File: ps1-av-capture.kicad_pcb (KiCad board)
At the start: 4 copper layers, 100 x 80 mm, 237 parts, among them J1 AV_PIGTAIL, J2 USB3_B, J3 USB_C_AUDIO, J4 JTAG, J5 UART, SW1 RESET, U1 TVP7002PZP, U10 TLV75733PDBVR, U11 TLV75533PDBVR, U12 PCM2903CDBR, U2 CYUSB3014-BZXI, U3 24LC1025-I/SN, U4 24LC1025-I/SN, U5 TPS563201DDCR, U6 TPS563201DDCR, U7 TPS563201DDCR, U8 TLV75519PDBVR, U9 TLV75519PDBVR, X1 27MHz, Y1 19.2MHz, Y2 12MHz

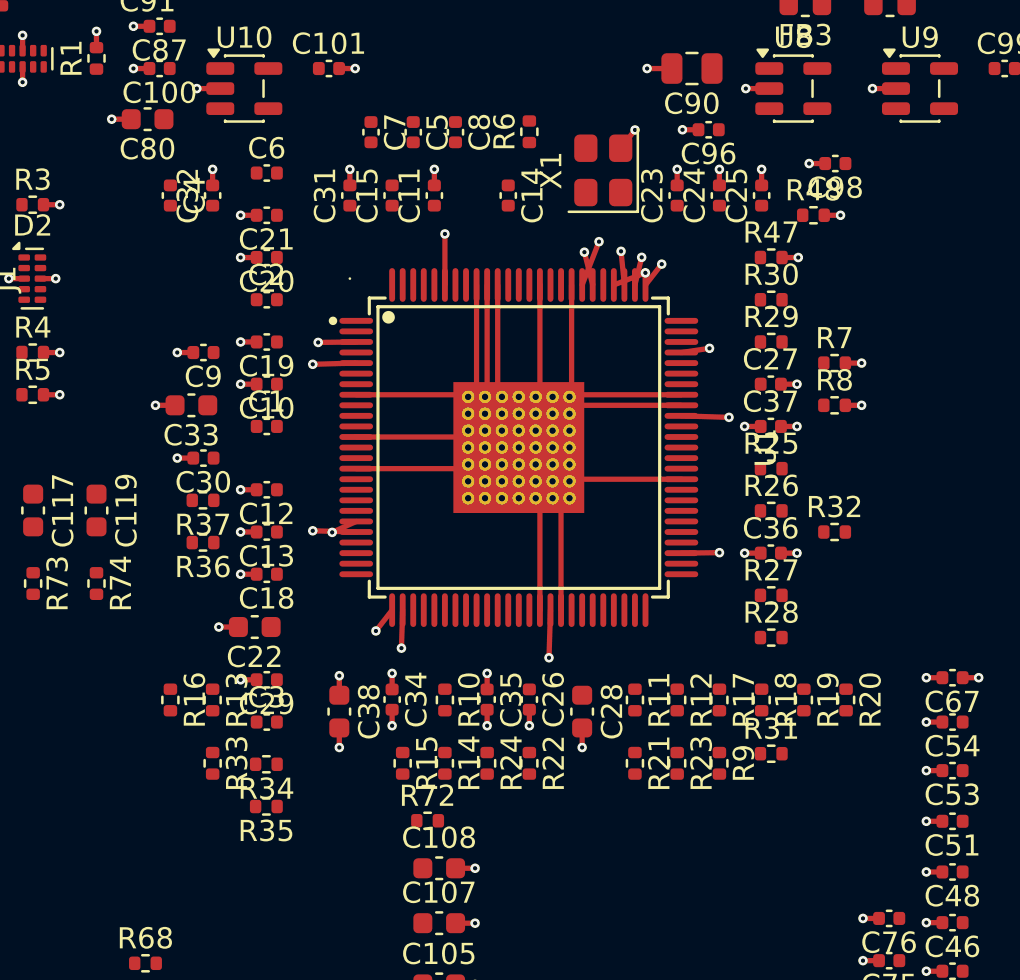
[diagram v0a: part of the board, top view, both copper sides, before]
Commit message: Layout: 22R series terminations hand-placed in pin order
The autoplacer scattered the 34 data/sync terminations around U1, some on the
far side from U2. They now sit just outside U1's escape ring in pin order (B/G
and DATACLK in a row under the south pins, R in a column east, syncs west), so
each bus fans out on L1 with no crossings before the scripted GPIF run.
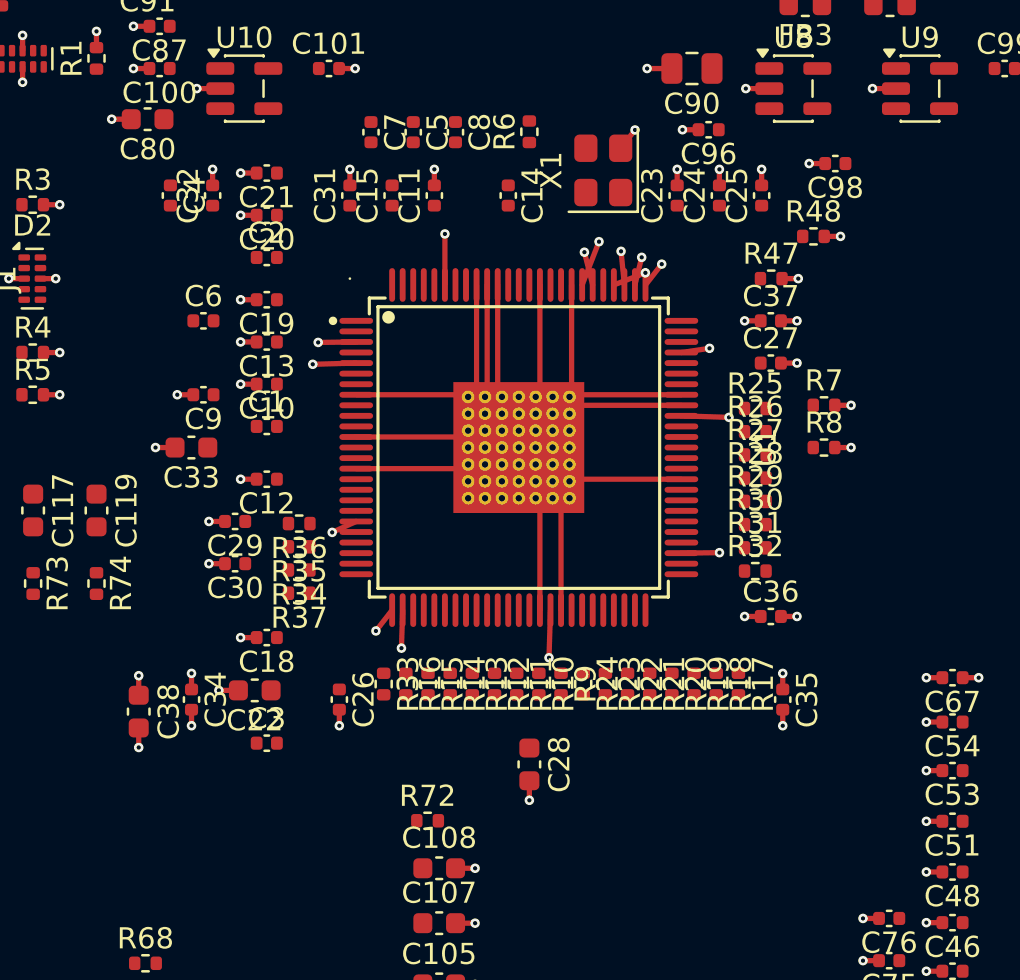
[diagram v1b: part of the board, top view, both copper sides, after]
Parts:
- moved C35 14.0 mm to (145.5, 137.9)
- moved R35 12.4 mm to (122.6, 130.7)
- moved R13 12.3 mm to (130.8, 137.2)
- moved R16 11.2 mm to (127.7, 137.2)
- moved R30 10.7 mm to (144.2, 129.7)
- moved R31 9.78 mm to (144.2, 130.8)
- moved C34 9.50 mm to (117.5, 137.9)
- moved C38 9.50 mm to (115.0, 138.5)
- moved R34 9.33 mm to (122.6, 131.8)
- moved C13 9.00 mm to (121.1, 121.0)
- moved C26 9.00 mm to (124.5, 137.9)
- moved R33 8.93 mm to (126.6, 137.2)
- moved R12 8.68 mm to (131.8, 137.2)
- moved R9 8.39 mm to (135.0, 137.2)
- moved R20 8.28 mm to (140.2, 137.2)
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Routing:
- net GND: track 235.9 -> 233.9 mm, vias 178 -> 177

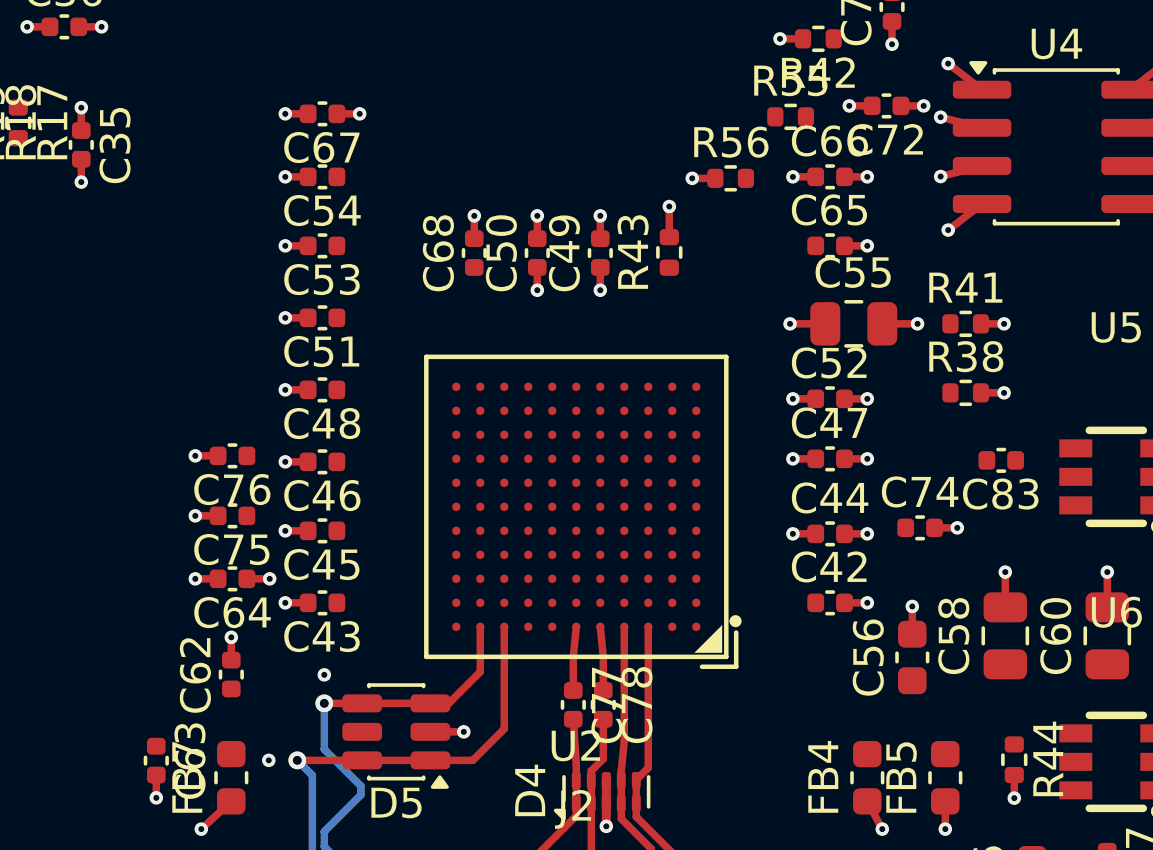
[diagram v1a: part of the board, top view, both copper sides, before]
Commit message: Layout: U2 plane decoupling on B.Cu
The 16 plane-only 0402 caps around the FX3 move to the back at the same spot,
so the F.Cu ring around U2 is free for the BGA escape and the GPIF bundle.
fanout.py stubs a back-side pad on B.Cu.
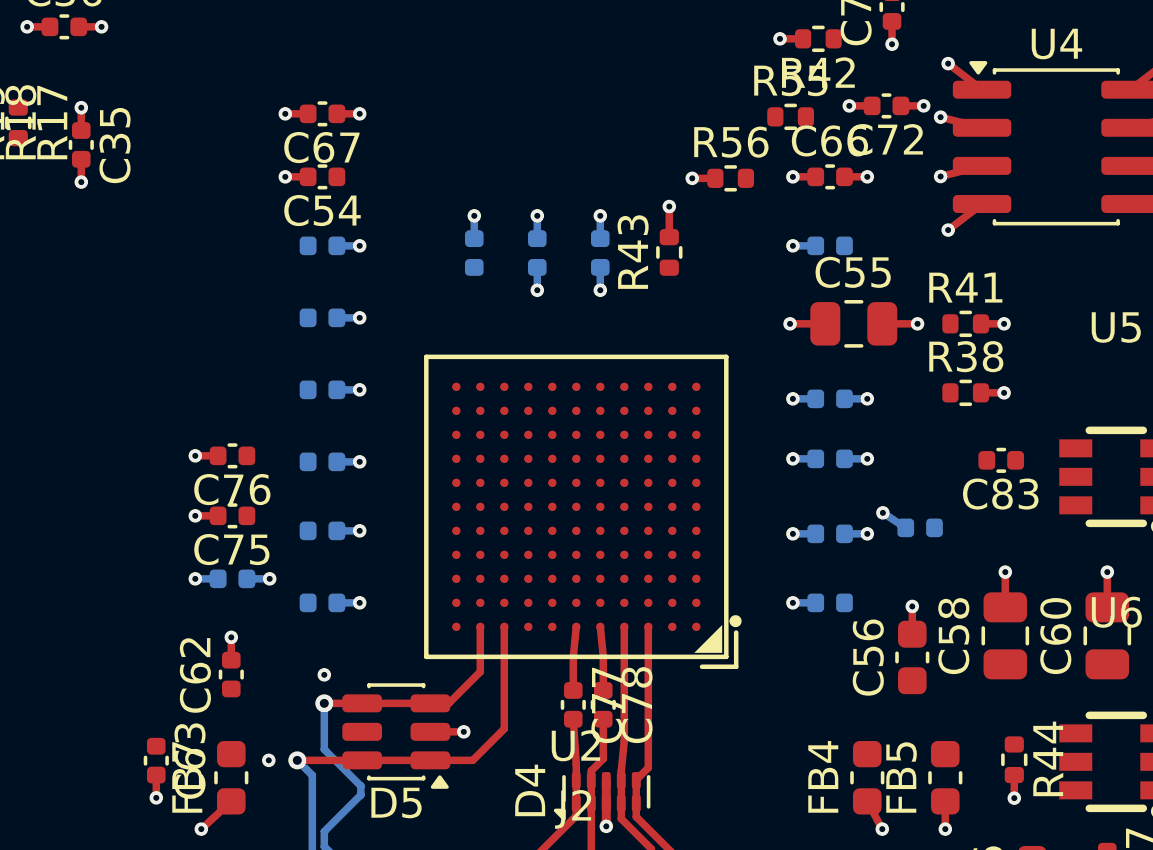
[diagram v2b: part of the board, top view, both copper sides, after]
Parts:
- C42, C43, C44, C45, C46, C47, C48, C49, C50, C51, C52, C53, C64, C65, C68, C74: moved to B.Cu
- turned C42 to 180 degrees
- turned C43 to 0 degrees
- turned C44 to 180 degrees
- turned C45 to 0 degrees
- turned C46 to 0 degrees
- turned C47 to 180 degrees
- turned C48 to 0 degrees
- turned C51 to 0 degrees
- turned C52 to 180 degrees
- turned C53 to 0 degrees
- turned C64 to 0 degrees
- turned C65 to 180 degrees
- turned C74 to 180 degrees

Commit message: Layout: +1V2 island reaches the west decaps
The +1V2 L3 region now starts at x=51 so the back-side +1V2 caps west of U2
can drop their vias onto it. Fanout leaves 41 pads for the router (was 47).
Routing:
- net +1V2: track 12.5 -> 18.5 mm, vias 12 -> 19

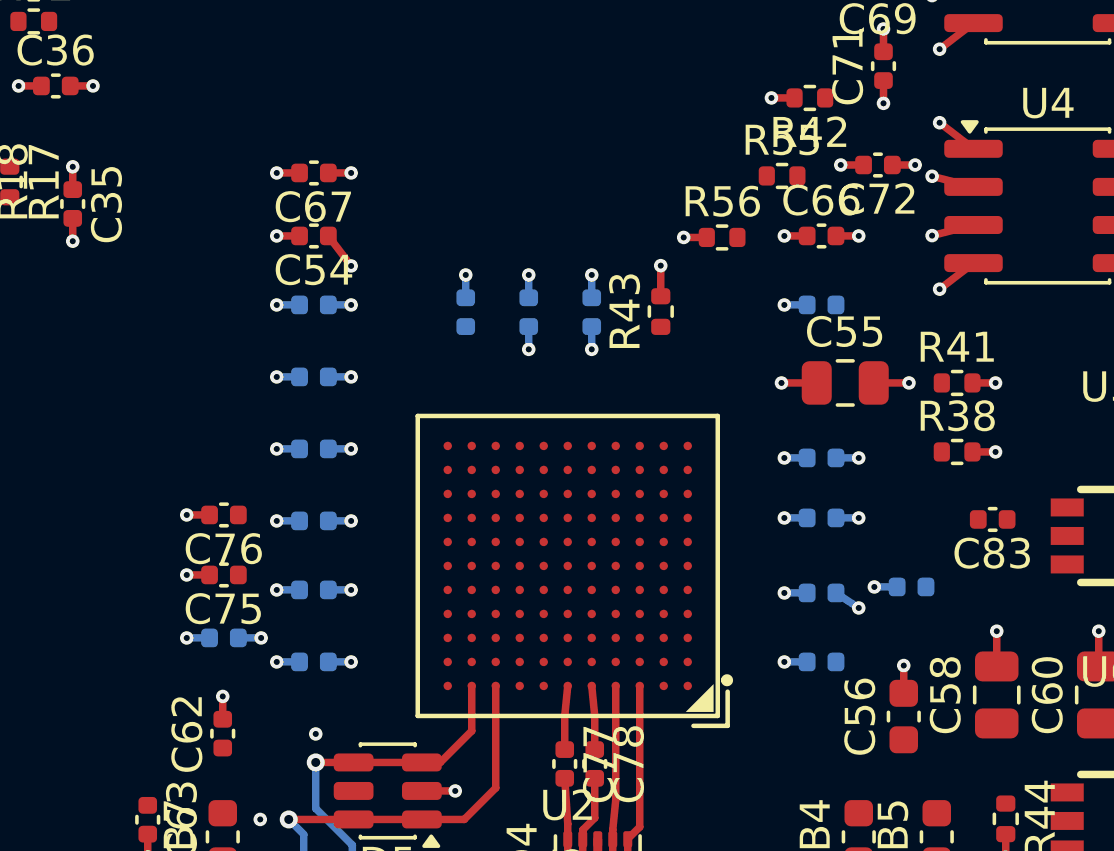
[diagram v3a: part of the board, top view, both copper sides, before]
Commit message: Layout: U2's +3V3 decaps out of the +1V2 island
Five back-side +3V3 caps sat where L3 is +1V2, so their vias had nothing to
land on. They now sit in a row just north of the island, +3V3 pad up. Every
decap around U2 reaches its planes; fanout leaves 37 pads for the router.
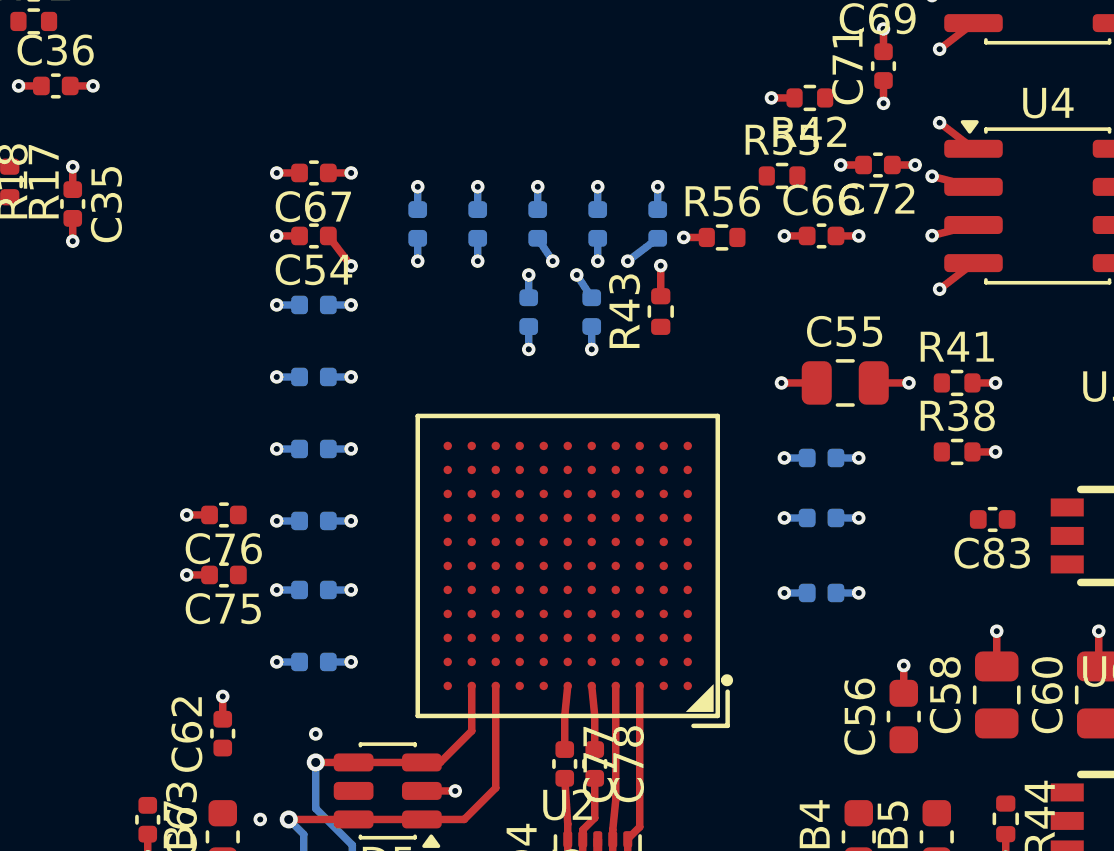
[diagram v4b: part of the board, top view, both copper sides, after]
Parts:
- moved C74 20.4 mm to (157.0, 138.6), turned to -90 degrees
- moved C64 18.6 mm to (163.0, 138.6), turned to -90 degrees
- moved C42 15.6 mm to (165.0, 138.6), turned to -90 degrees
- moved C65 9.84 mm to (161.0, 138.6), turned to -90 degrees
- moved C68 2.97 mm to (159.0, 138.6), turned to -90 degrees
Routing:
- net +3V3: track 40.8 -> 43.9 mm, vias 37 -> 41
- net GND: track 233.9 -> 234.7 mm

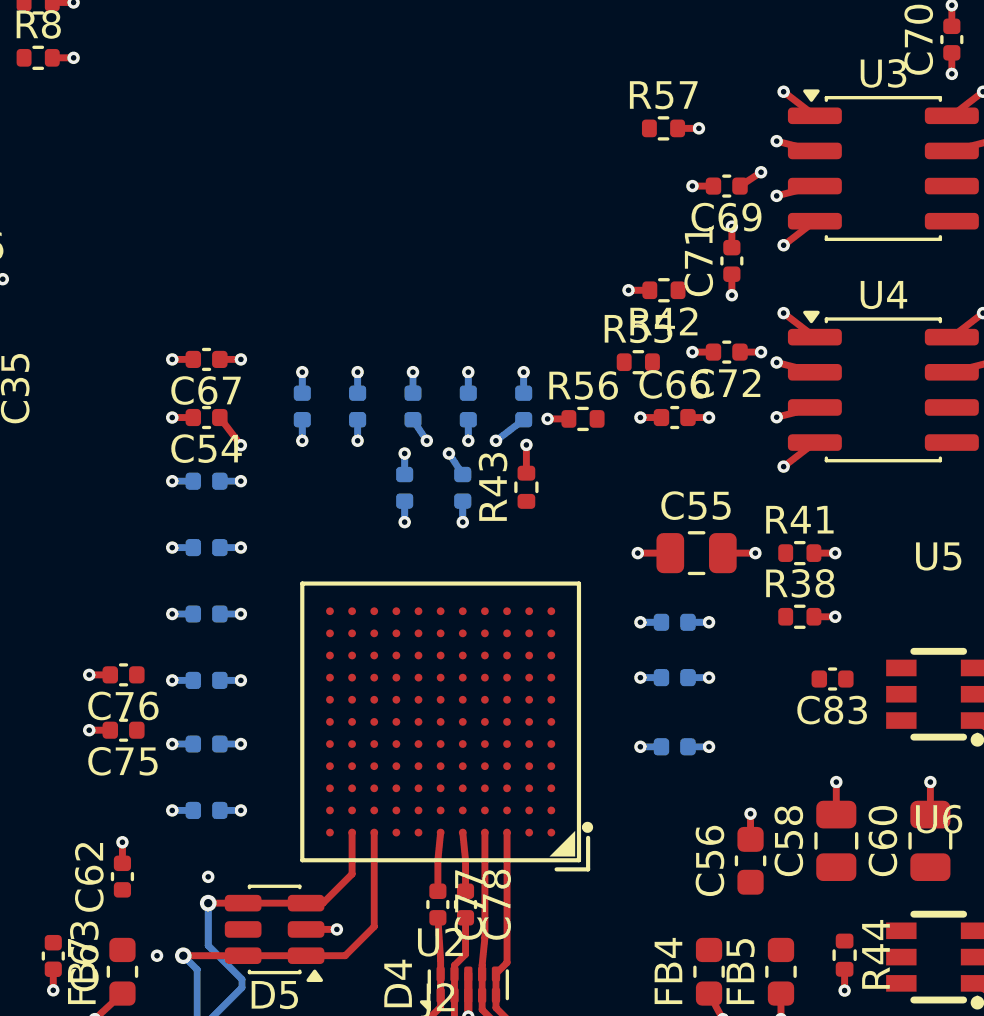
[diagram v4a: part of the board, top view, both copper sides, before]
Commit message: Layout: FX3 plane balls fanned out, +3V3 channels through the +1V2 island
fanout.py counted BGA balls as vias in its same-net hole-to-hole check, so
every dogbone was rejected by its own ball (0.57 mm < 0.7 mm) and no U2 plane
ball was ever fanned. The spacing check now covers vias only: fanout leaves 7
pads for the router (was 37).

U2's six +3V3 balls sit over the L3 +1V2 island; each one's dogbone via now
lands in a +3V3 channel running out past the island edge to the main pour.
DRC lists no unconnected +3V3 or U2 plane pad.
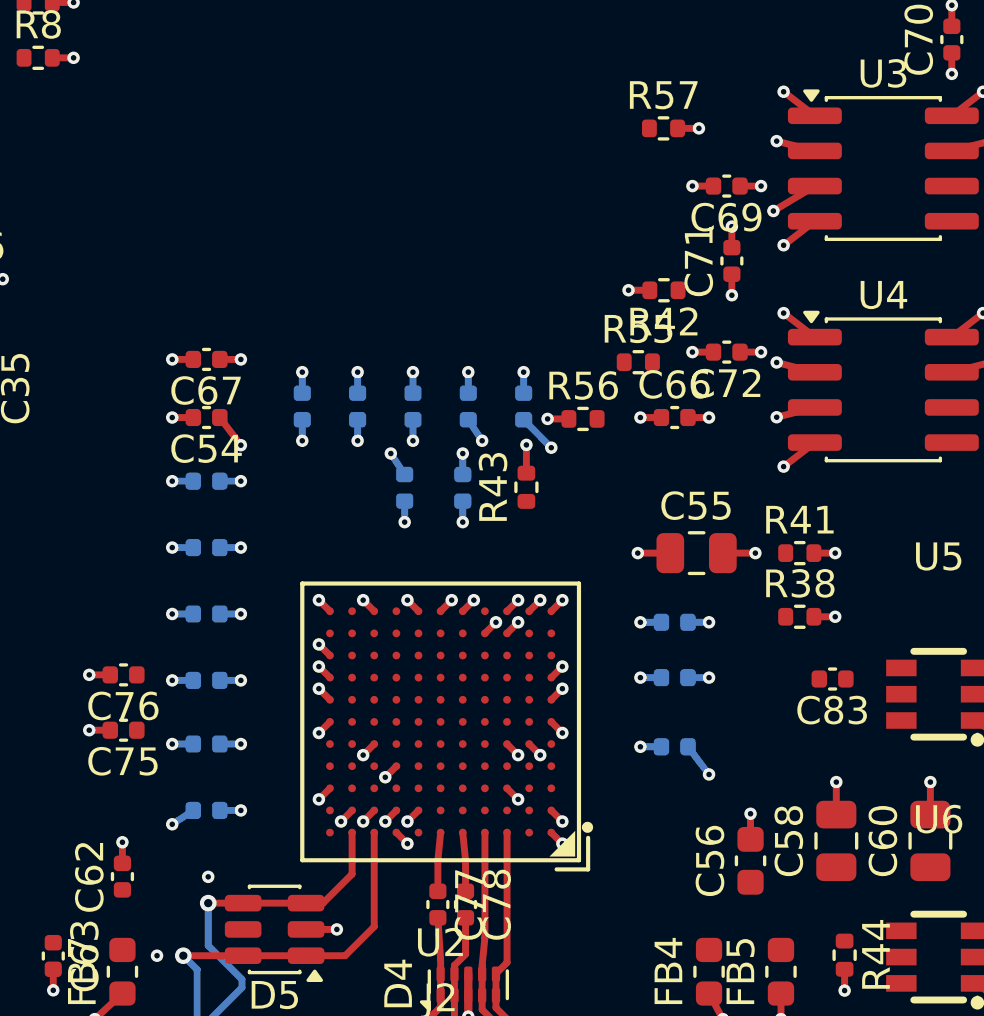
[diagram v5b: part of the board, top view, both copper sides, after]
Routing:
- net GND: track 234.7 -> 243.9 mm, vias 177 -> 193
- net +1V2: track 18.3 -> 23.5 mm, vias 19 -> 27
- net +3V3: track 43.9 -> 47.4 mm, vias 41 -> 47
